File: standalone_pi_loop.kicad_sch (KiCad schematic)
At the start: 25 parts, among them J1 Conn_01x10_Pin, J10 Conn_Coaxial, J2 Conn_01x10_Pin, J3 Conn_01x02, J4 Conn_01x05, J7 Conn_Coaxial, J9 Conn_Coaxial, U1 AD823, U2 AD620

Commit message: R4 -> 47R, a more common std value. added inst. amp gain formula to schematic, added PI gain adjust trimpot to schematic
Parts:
- added RV2: 10k, Potentiometer_THT:Potentiometer_Bourns_3296W_Vertical, symbol Device:R_Potentiometer_Small
- R4: value 50 -> 47R
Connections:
- net at R3.1: now also RV2.1, RV2.2; no longer JP1.2 (C)
- new net: JP1.2 (C), RV2.3
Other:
- note added: "G=106 @ R_G=470R"
- note added: "P Gain adjust"
- note added: "PI Gain adjust"
- note added: "R_G = 49.4 kOhm / (G-1) G = 1+49.4kOhm/R_G"
- moved on the sheet: J10, JP1, R3
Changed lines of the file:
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@@
 	)
 	(junction
-		(at 27.305 103.505)
+		(at 109.22 69.85)
 		(diameter 0)
 		(color 0 0 0 0)
 	)
 	(junction
-		(at 27.305 85.725)
+		(at 121.92 69.85)
 		(diameter 0)
 		(color 0 0 0 0)
 	)
 	(junction
-		(at 236.855 69.215)
+		(at 27.305 103.505)
 		(diameter 0)
 		(color 0 0 0 0)
 	)
 	(junction
-		(at 121.92 69.85)
+		(at 27.305 85.725)
+		(diameter 0)
+		(color 0 0 0 0)
+	)
+	(junction
+		(at 236.855 69.215)
 		(diameter 0)
 		(color 0 0 0 0)
@@
 		)
 	)
-	(wire
-		(pts
-			(xy 120.015 69.85) (xy 121.92 69.85)
-		)
-		(stroke
-			(width 0)
-			(type default)
-		)
-	)
 	(polyline
 		(pts
@@
 	(wire
 		(pts
-			(xy 89.535 60.325) (xy 89.535 64.77)
+			(xy 109.22 69.85) (xy 106.68 69.85)
+		)
+		(stroke
+			(width 0)
+			(type default)
+		)
+	)
+	(wire
+		(pts
+			(xy 88.9 60.325) (xy 88.9 64.77)
 		)
 		(stroke
@@
 	(wire
 		(pts
+			(xy 109.22 67.31) (xy 109.22 69.85)
+		)
+		(stroke
+			(width 0)
+			(type default)
+		)
+	)
+	(wire
+		(pts
 			(xy 236.855 67.31) (xy 236.855 69.215)
 		)
@@
 	(wire
 		(pts
+			(xy 92.71 69.85) (xy 101.6 69.85)
+		)
+		(stroke
+			(width 0)
+			(type default)
+		)
+	)
+	(wire
+		(pts
 			(xy 211.455 52.07) (xy 211.455 54.61)
 		)
@@
 	(wire
 		(pts
+			(xy 119.38 69.85) (xy 121.92 69.85)
+		)
+		(stroke
+			(width 0)
+			(type default)
+		)
+	)
+	(wire
+		(pts
 			(xy 229.235 64.77) (xy 208.915 64.77)
 		)
@@
 	(wire
 		(pts
+			(xy 109.22 69.85) (xy 114.3 69.85)
+		)
+		(stroke
+			(width 0)
+			(type default)
+		)
+	)
+	(wire
+		(pts
 			(xy 42.545 46.355) (xy 40.64 46.355)
 		)
@@
 	(wire
 		(pts
-			(xy 93.345 69.85) (xy 114.935 69.85)
+			(xy 104.14 67.31) (xy 109.22 67.31)
 		)
 		(stroke
@@
 		)
 	)
+	(text "G=106 @ R_G=470R"
+		(exclude_from_sim no)
+		(at 217.678 31.242 0)
+		(effects
+			(font
+				(size 1.27 1.27)
+			)
+		)
+	)
+	(text "PI Gain adjust"
+		(exclude_from_sim no)
+		(at 103.632 61.976 0)
+		(effects
+			(font
+				(size 1.27 1.27)
+			)
+		)
+	)
 	(text "Tie pins of unused op-amp"
 		(exclude_from_sim no)
@@
 	(text "Option for on-board or\noff-board in-loop v"
 		(exclude_from_sim no)
-		(at 101.6 64.135 0)
+		(at 73.533 64.008 0)
 		(effects
 			(font
@@
 	(text "external In-loop V"
 		(exclude_from_sim no)
-		(at 77.47 83.82 0)
+		(at 76.835 83.82 0)
 		(effects
 			(font
@@
 		)
 	)
+	(text "P Gain adjust"
+		(exclude_from_sim no)
+		(at 145.542 54.102 0)
+		(effects
+			(font
+				(size 1.27 1.27)
+			)
+		)
+	)
 	(text "Two headers allow for dasiy chaining across boards"
 		(exclude_from_sim no)
@@
 		)
 	)
+	(text "R_G = 49.4 kOhm / (G-1)\nG 	= 1+49.4kOhm/R_G"
+		(exclude_from_sim no)
+		(at 207.518 27.94 0)
+		(effects
+			(font
+				(size 1.27 1.27)
+			)
+			(justify left)
+		)
+	)
 	(text "Unused op-amp"
 		(exclude_from_sim no)
@@
 	)
 	(label "on_board_in_loop_v"
-		(at 89.535 60.325 180)
+		(at 88.9 60.325 180)
 		(fields_autoplaced yes)
 		(effects
@@
 	(symbol
 		(lib_id "Connector:Conn_Coaxial")
-		(at 89.535 80.01 270)
+		(at 88.9 80.01 270)
 		(unit 1)
 		(exclude_from_sim no)
@@
 		(fields_autoplaced yes)
 		(property "Reference" "J10"
-			(at 87.9717 83.82 0)
+			(at 87.3367 83.82 0)
 			(effects
 				(font
@@
 		)
 		(property "Value" "Conn_Coaxial"
-			(at 90.5117 83.82 0)
+			(at 89.8767 83.82 0)
 			(effects
 				(font
@@
 		)
 		(property "Footprint" "Connector_Coaxial:SMA_Amphenol_132289_EdgeMount"
-			(at 89.535 80.01 0)
+			(at 88.9 80.01 0)
 			(effects
 				(font
@@
 		)
 		(property "Datasheet" "~"
-			(at 89.535 80.01 0)
+			(at 88.9 80.01 0)
 			(effects
 				(font
@@
 		)
 		(property "Description" "coaxial connector (BNC, SMA, SMB, SMC, Cinch/RCA, LEMO, ...)"
-			(at 89.535 80.01 0)
+			(at 88.9 80.01 0)
 			(effects
 				(font
@@
 		)
 		(property "Digikey PN" "ACX1426-ND"
-			(at 89.535 80.01 0)
+			(at 88.9 80.01 0)
 			(effects
 				(font
@@
 	)
 	(symbol
+		(lib_id "Device:R_Potentiometer_Small")
+		(at 104.14 69.85 270)
+		(mirror x)
+		(unit 1)
+		(exclude_from_sim no)
+		(in_bom yes)
+		(on_board yes)
+		(dnp no)
+		(property "Reference" "RV2"
+			(at 103.886 64.008 90)
+			(effects
+				(font
+					(size 1.27 1.27)
+				)
+			)
+		)
+		(property "Value" "10k"
+			(at 104.14 66.04 90)
+			(effects
+				(font
+					(size 1.27 1.27)
+				)
+			)
+		)
+		(property "Footprint" "Potentiometer_THT:Potentiometer_Bourns_3296W_Vertical"
+			(at 104.14 69.85 0)
+			(effects
+				(font
+					(size 1.27 1.27)
+				)
+				(hide yes)
+			)
+		)
+		(property "Datasheet" "~"
+			(at 104.14 69.85 0)
+			(effects
+				(font
+					(size 1.27 1.27)
+				)
+				(hide yes)
+			)
+		)
+		(property "Description" "Potentiometer"
+			(at 104.14 69.85 0)
+			(effects
+				(font
+					(size 1.27 1.27)
+				)
+				(hide yes)
+			)
+		)
+		(pin "2"
+		)
+		(pin "1"
+		)
+		(pin "3"
+		)
+		(instances
+			(project "standalone_pi_loop"
+				(path "/9c6abd11-1aac-4f08-8b79-cac116854bcb"
+					(reference "RV2")
+					(unit 1)
+				)
+			)
+		)
+	)
+	(symbol
 		(lib_id "power:GND")
 		(at 57.15 138.43 90)
@@
 	(symbol
 		(lib_id "power:GND")
-		(at 84.455 80.01 270)
+		(at 83.82 80.01 270)
 		(unit 1)
 		(exclude_from_sim no)
@@
 		(dnp no)
 		(property "Reference" "#PWR037"
-			(at 78.105 80.01 0)
+			(at 77.47 80.01 0)
 			(effects
 				(font
@@
 		)
 		(property "Value" "GND"
-			(at 79.375 80.01 90)
+			(at 78.74 80.01 90)
 			(effects
 				(font
@@
 		)
 		(property "Footprint" ""
-			(at 84.455 80.01 0)
+			(at 83.82 80.01 0)
 			(effects
 				(font
@@
 		)
 		(property "Datasheet" ""
-			(at 84.455 80.01 0)
+			(at 83.82 80.01 0)
 			(effects
 				(font
@@
 		)
 		(property "Description" "Power symbol creates a global label with name \"GND\" , ground"
-			(at 84.455 80.01 0)
+			(at 83.82 80.01 0)
 			(effects
 				(font
@@
 			)
 		)
-		(property "Value" "50"
+		(property "Value" "47R"
 			(at 160.655 69.85 90)
 			(effects
@@
 	(symbol
 		(lib_id "Device:R_Small")
-		(at 117.475 69.85 90)
+		(at 116.84 69.85 90)
 		(unit 1)
 		(exclude_from_sim no)
@@
 		(fields_autoplaced yes)
 		(property "Reference" "R3"
-			(at 117.475 64.77 90)
+			(at 116.84 64.77 90)
 			(effects
 				(font
@@
 		)
 		(property "Value" "3k3"
-			(at 117.475 67.31 90)
+			(at 116.84 67.31 90)
 			(effects
 				(font
@@
 		)
 		(property "Footprint" "Resistor_THT:R_Axial_DIN0207_L6.3mm_D2.5mm_P10.16mm_Horizontal"
-			(at 117.475 69.85 0)
+			(at 116.84 69.85 0)
 			(effects
 				(font
@@
 		)
 		(property "Datasheet" "~"
-			(at 117.475 69.85 0)
+			(at 116.84 69.85 0)
 			(effects
 				(font
@@
 		)
 		(property "Description" "Resistor, small symbol"
-			(at 117.475 69.85 0)
+			(at 116.84 69.85 0)
 			(effects
 				(font
@@
 	(symbol
 		(lib_id "Jumper:SolderJumper_3_Open")
-		(at 89.535 69.85 90)
+		(at 88.9 69.85 90)
 		(unit 1)
 		(exclude_from_sim yes)
@@
 		(dnp no)
 		(property "Reference" "JP1"
-			(at 92.075 66.675 90)
+			(at 91.44 66.675 90)
 			(effects
 				(font
@@
 		)
 		(property "Value" "SolderJumper_3_Open"
-			(at 83.82 69.85 0)
+			(at 83.185 69.85 0)
 			(effects
 				(font
@@
 		)
 		(property "Footprint" "Jumper:SolderJumper-3_P1.3mm_Open_Pad1.0x1.5mm"
-			(at 89.535 69.85 0)
+			(at 88.9 69.85 0)
 			(effects
 				(font
@@
 		)
 		(property "Datasheet" "~"
-			(at 89.535 69.85 0)
+			(at 88.9 69.85 0)
 			(effects
 				(font
@@
 		)
 		(property "Description" "Solder Jumper, 3-pole, open"
-			(at 89.535 69.85 0)
+			(at 88.9 69.85 0)
 			(effects
 				(font

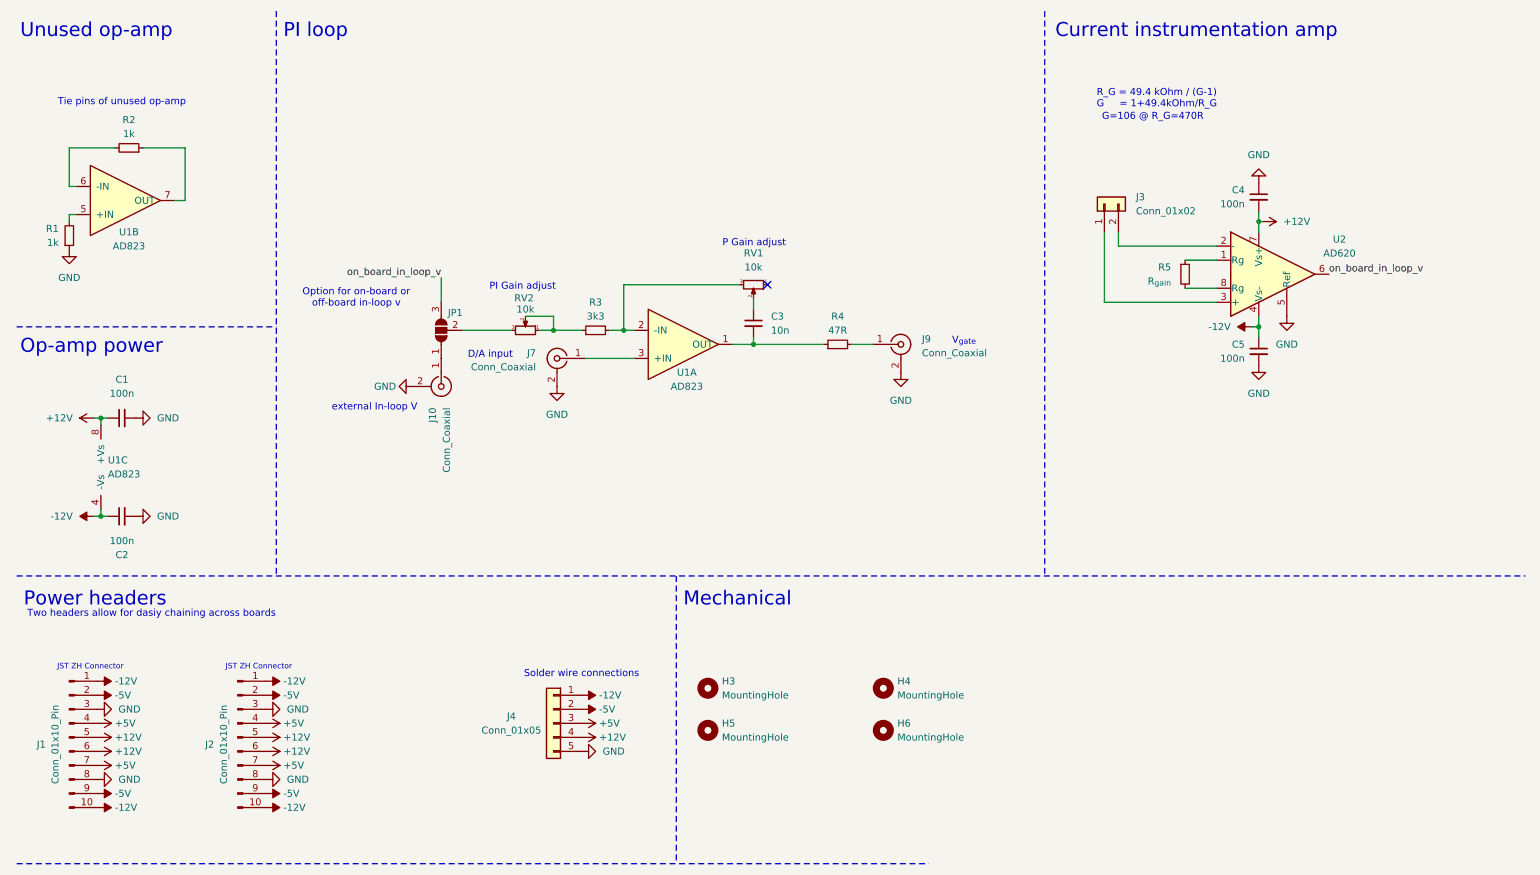
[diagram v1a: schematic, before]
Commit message: started schematic changes for V2, added todo list
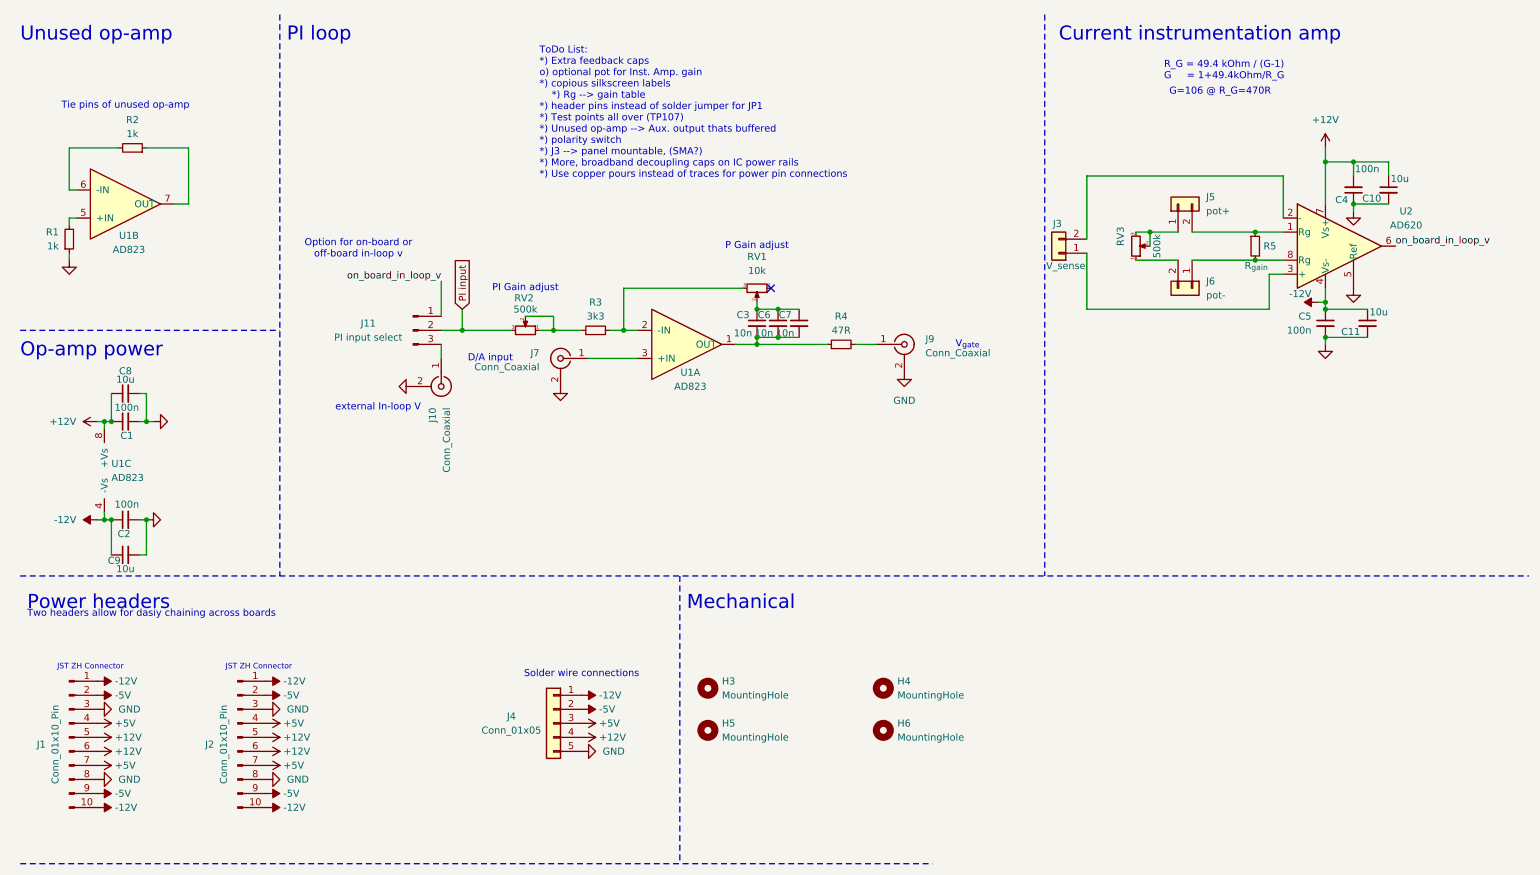
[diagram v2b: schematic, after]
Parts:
- removed JP1: SolderJumper_3_Open, Jumper:SolderJumper-3_P1.3mm_Open_Pad1.0x1.5mm, symbol Jumper:SolderJumper_3_Open
- added C10, C11, C8, C9: 10u, Capacitor_THT:C_Disc_D4.3mm_W1.9mm_P5.00mm, symbol Device:C_Small
- added C6, C7: 10n, Capacitor_THT:C_Disc_D4.3mm_W1.9mm_P5.00mm, symbol Device:C_Small
- added J11: PI input select, Connector_PinHeader_2.54mm:PinHeader_1x03_P2.54mm_Vertical, symbol Connector:Conn_01x03_Pin
- added J5: pot+, Connector_PinHeader_2.54mm:PinHeader_1x02_P2.54mm_Vertical, symbol Connector_Generic:Conn_01x02
- added J6: pot-, Connector_PinHeader_2.54mm:PinHeader_1x02_P2.54mm_Vertical, symbol Connector_Generic:Conn_01x02
- added RV3: 500k, Potentiometer_THT:Potentiometer_Bourns_3296W_Vertical, symbol Device:R_Potentiometer_Small
- J3: value Conn_01x02 -> V_sense
- RV2: value 10k -> 500k
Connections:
- net +12V: now also C10.1, C8.1
- net -12V: now also C11.1, C9.1
- net GND: now also C10.2, C11.2, C8.2, C9.2
- net on_board_in_loop_v: now also J11.1 (Pin_1)
- net at R5.1, U2.1 (Rg): now also J5.2 (Pin_2)
- net at R5.2, U2.8 (Rg): now also J6.1 (Pin_1)
- net at J10.1 (In): now also J11.3 (Pin_3)
- net at C3.1, RV1.2: now also C6.1, C7.1
- net at C3.2, R4.1, U1.1 (OUT): now also C6.2, C7.2
- net PI input: now reaches RV2.3
- net PI input: now also J11.2 (Pin_2)
- new net: J6.2 (Pin_2), RV3.1
- new net: J5.1 (Pin_1), RV3.2, RV3.3
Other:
- note added: "ToDo List: *) Extra feedback caps o) optional pot for Inst. Amp. gain *) copious silkscreen labels *) Rg --> gain table *) header pins instead of solder jumper for JP1 *) Test points all over (TP107) *) Unused op-amp --> Aux. output thats buffered *) polarity switch *) J3 --> panel mountable, (SMA?) *) More, broadband decoupling caps on IC power rails *) Use copper pours instead of traces for pow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"
- moved on the sheet: C1, C2, C3, C4, C5, J3, J7, J9, R1, R2, R4, R5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

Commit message: Draft of layout + routing. Added alt out, LPF on setpoint.
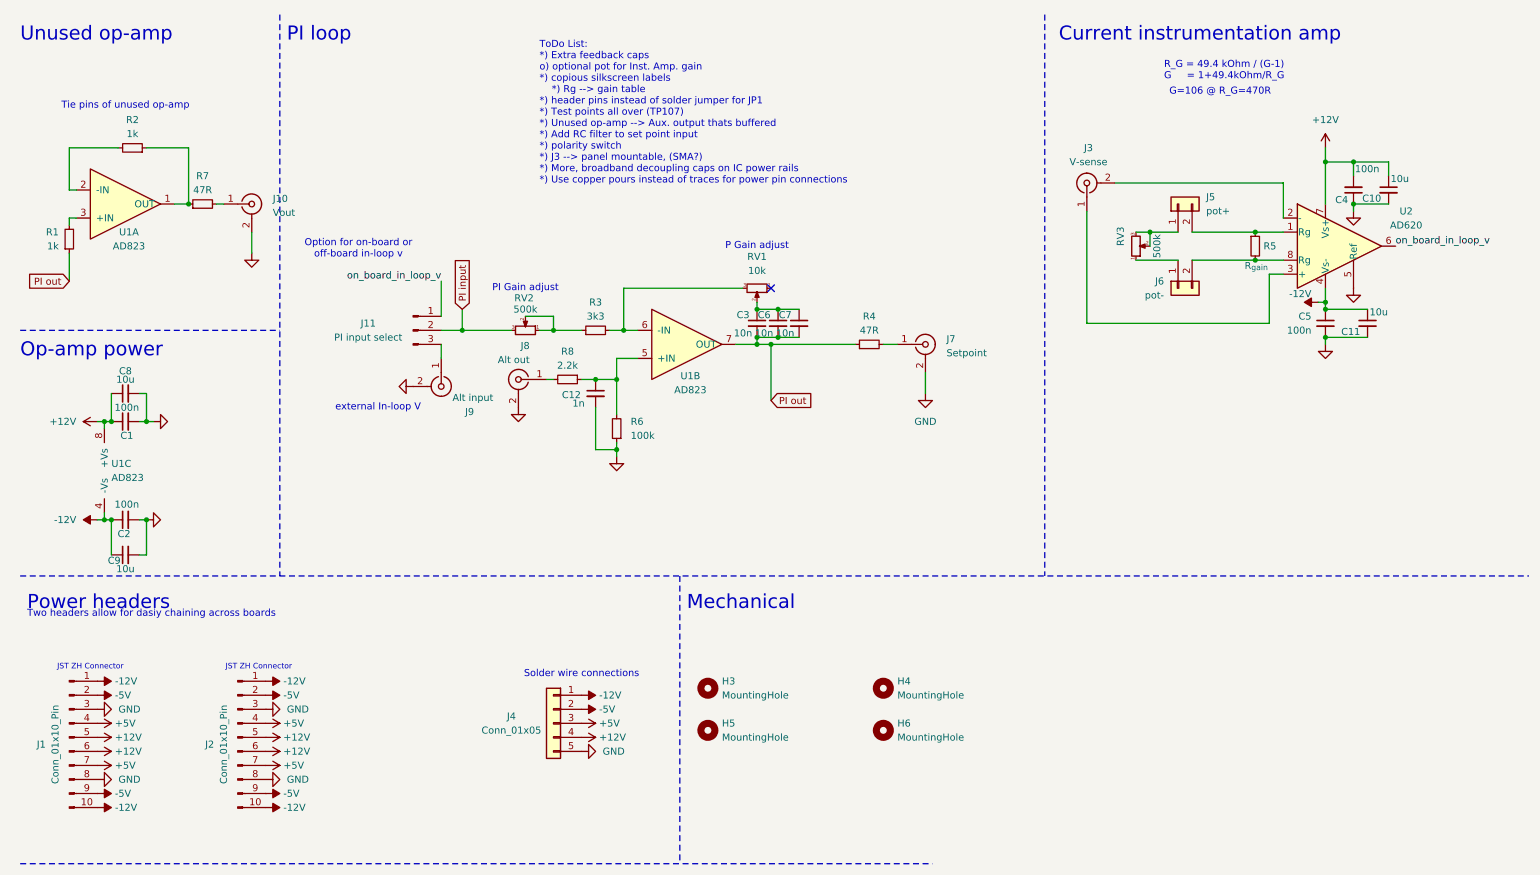
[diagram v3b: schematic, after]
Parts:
- removed J3: V_sense, Connector_Wire:SolderWire-1sqmm_1x02_P5.4mm_D1.4mm_OD2.7mm, symbol Connector_Generic:Conn_01x02
- added C12: 1n, Capacitor_THT:C_Disc_D4.3mm_W1.9mm_P5.00mm, symbol Device:C_Small
- added J8: Alt out, Connector_Coaxial:SMA_Amphenol_132289_EdgeMount, symbol Connector:Conn_Coaxial
- added J9: Alt input, Connector_Coaxial:SMA_Amphenol_132289_EdgeMount, symbol Connector:Conn_Coaxial
- added R6: 100k, Resistor_THT:R_Axial_DIN0207_L6.3mm_D2.5mm_P10.16mm_Horizontal, symbol Device:R_Small
- added R7: 47R, Resistor_THT:R_Axial_DIN0207_L6.3mm_D2.5mm_P10.16mm_Horizontal, symbol Device:R_Small
- added R8: 2.2k, Resistor_THT:R_Axial_DIN0207_L6.3mm_D2.5mm_P10.16mm_Horizontal, symbol Device:R_Small
- J10: value Conn_Coaxial -> Vout
- J3: renamed from J9; value Conn_Coaxial -> V-sense
- J7: value Conn_Coaxial -> Setpoint
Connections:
- net GND: now also C12.2, J8.2 (Ext), J9.2 (Ext), R6.1; no longer J3.2 (Ext), R1.1
- net at U2.2 (-): now also J3.2 (Ext)
- net at U2.3 (+): now also J3.1 (In)
- net at R5.2, U2.8 (Rg): now also J6.2 (Pin_2); no longer J6.1 (Pin_1)
- net at U1.5 (+IN): now also C12.1, R6.2, R8.1; no longer R1.2
- net at U1.6 (-IN): now also R3.2, RV1.3; no longer R2.2
- net at R2.1: now also U1.1 (OUT), R7.1; no longer U1.7 (OUT)
- net at J10.1 (In): now also R7.2; no longer J11.3 (Pin_3)
- net at J7.1 (In): now also R4.2; no longer U1.3 (+IN)
- net PI out: now reaches C3.2, C6.2, C7.2, R4.1
- net PI out: now also R1.1, U1.7 (OUT); no longer U1.1 (OUT)
- net at RV3.1: now also J6.1 (Pin_1); no longer J6.2 (Pin_2)
- new net: J8.1 (In), R8.2
- new net: J11.3 (Pin_3), J9.1 (In)
- new net: R2.2, U1.2 (-IN)
- new net: R1.2, U1.3 (+IN)
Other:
- note added: "ToDo List: *) Extra feedback caps o) optional pot for Inst. Amp. gain *) copious silkscreen labels *) Rg --> gain table *) header pins instead of solder jumper for JP1 *) Test points all over (TP107) *) Unused op-amp --> Aux. output thats buffered *) Add RC filter to set point input *) polarity switch *) J3 --> panel mountable, (SMA?) *) More, broadband decoupling caps on IC power rails *) Use co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"
- note removed: "D/A input"
- note removed: "ToDo List: *) Extra feedback caps o) optional pot for Inst. Amp. gain *) copious silkscreen labels *) Rg --> gain table *) header pins instead of solder jumper for JP1 *) Test points all over (TP107) *) Unused op-amp --> Aux. output thats buffered *) polarity switch *) J3 --> panel mountable, (SMA?) *) More, broadband decoupling caps on IC power rails *) Use copper pours instead of traces for pow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"
- note removed: "V_{gate}"
- moved on the sheet: J10, J3, J6, J7, R4, U1A, U1B
